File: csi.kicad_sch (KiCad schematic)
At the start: 5 parts, among them J6 WE_68715014022

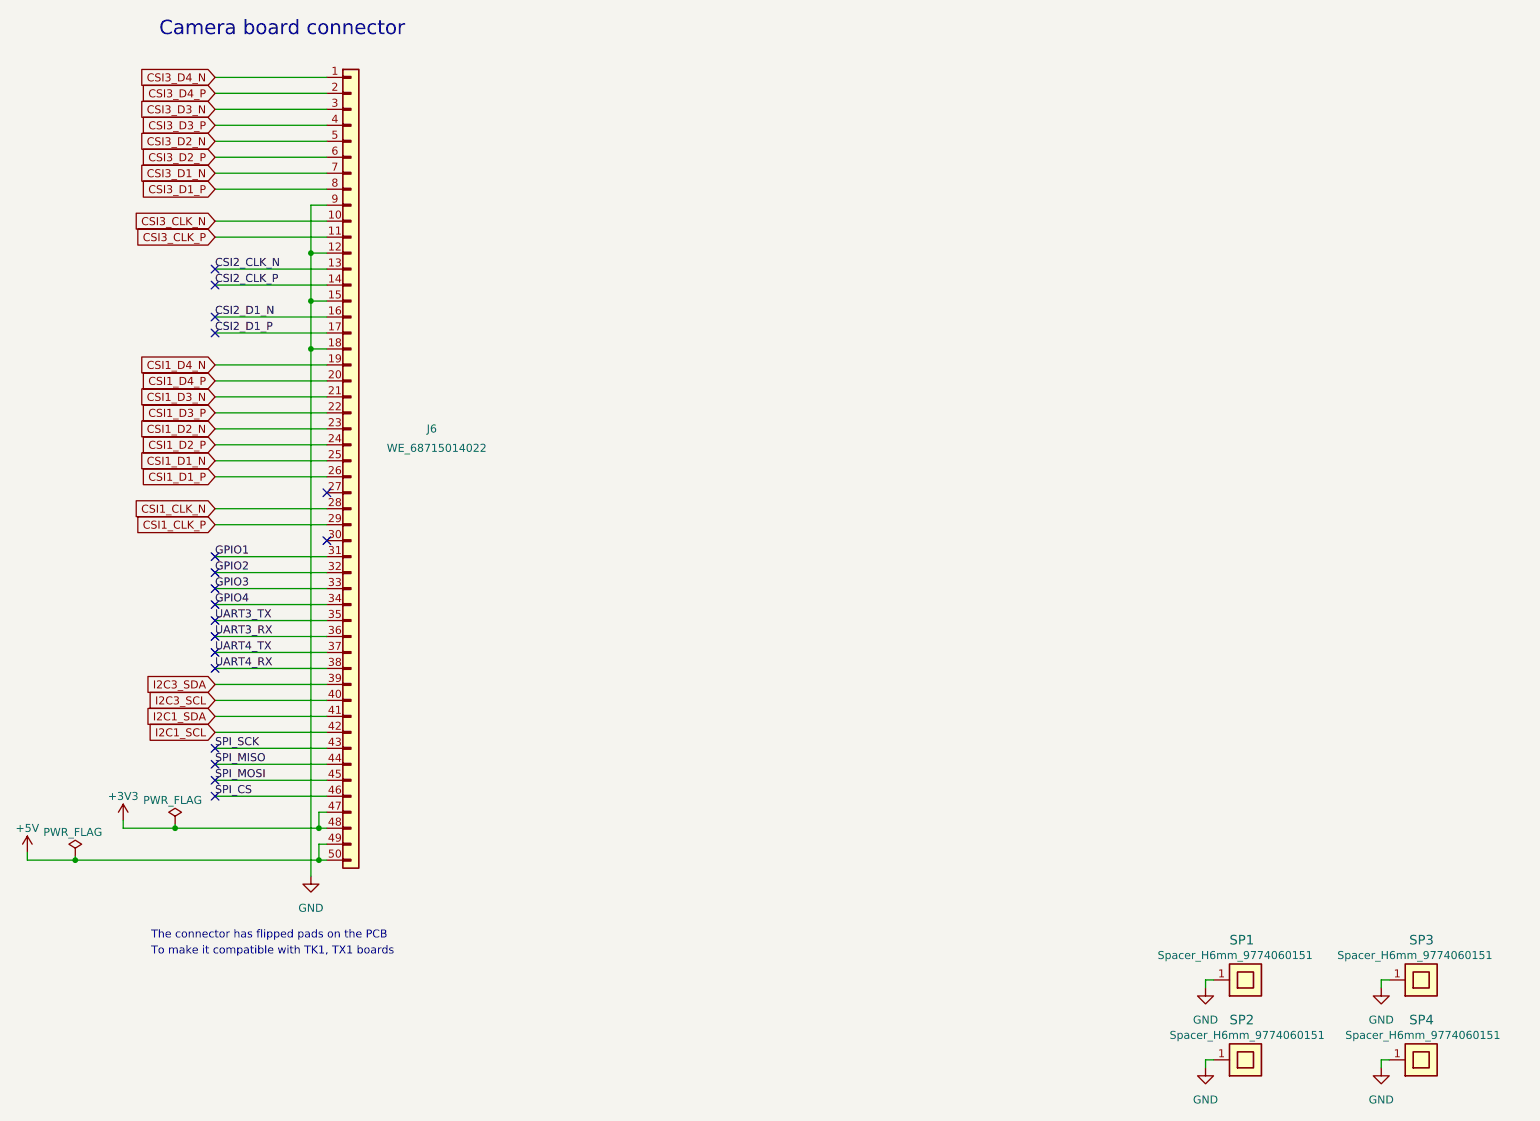
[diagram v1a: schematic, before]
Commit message: [#58304] Update symbols to global libs
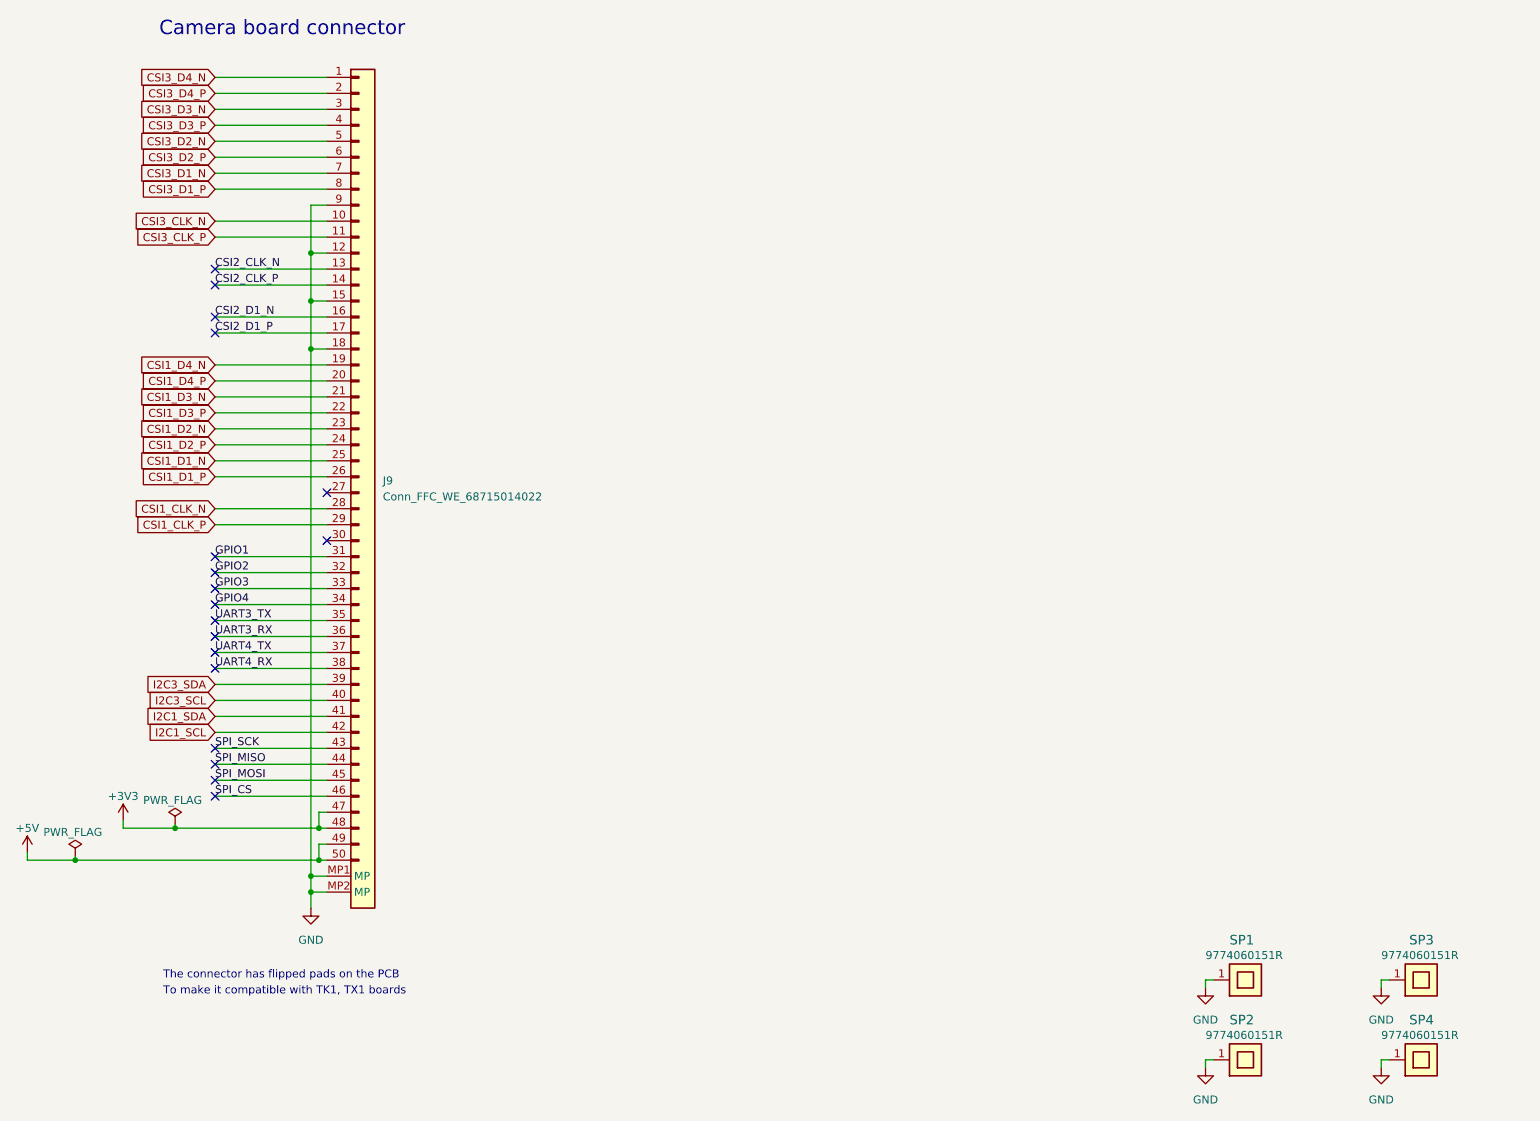
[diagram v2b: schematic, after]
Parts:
- removed J6: WE_68715014022, antmicro-hdmi-mipi-bridge-hw-footprints:WE_68715014022, symbol antmicro-hdmi-mipi-bridge-hw:WE_68715014022
- added J9: Conn_FFC_WE_68715014022, antmicro-footprints:Conn_FFC_WE_68715014x22, symbol antmicroFCCConnectors:Conn_FFC_WE_68715014022
- SP1, SP2, SP3, SP4: value Spacer_H6mm_9774060151 -> Spacer_Drill3.7mm_H6mm_9774060151R; footprint antmicro-hdmi-mipi-bridge-hw-footprints:Spacer_SMD_M2.5_H6mm_Wurth_9774060151 -> antmicro-footprints:Spacer_Drill3.7mm_H6mm_9774060151R; symbol antmicro-hdmi-mipi-bridge-hw:Spacer_H6mm_9774060151 -> antmicroMechanicalParts:Spacer_Drill3.7mm_H6mm_9774060151R; MPN 9774060151 -> 9774060151R
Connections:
- net +3V3: now also J9.47, J9.48
- net +5V: now also J9.49, J9.50
- net CSI1_CLK_N: now also J9.28
- net CSI1_CLK_P: now also J9.29
- net CSI1_D1_N: now also J9.25
- net CSI1_D1_P: now also J9.26
- net CSI1_D2_N: now also J9.23
- net CSI1_D2_P: now also J9.24
- net CSI1_D3_N: now also J9.21
- net CSI1_D3_P: now also J9.22
- net CSI1_D4_N: now also J9.19
- net CSI1_D4_P: now also J9.20
- net CSI2_CLK_N: now also J9.13
- net CSI2_CLK_P: now also J9.14
- net CSI2_D1_N: now also J9.16
- net CSI2_D1_P: now also J9.17
- net CSI3_CLK_N: now also J9.10
- net CSI3_CLK_P: now also J9.11
- net CSI3_D1_N: now also J9.7
- net CSI3_D1_P: now also J9.8
- net CSI3_D2_N: now also J9.5
- net CSI3_D2_P: now also J9.6
- net CSI3_D3_N: now also J9.3
- net CSI3_D3_P: now also J9.4
- net CSI3_D4_N: now also J9.1
- net CSI3_D4_P: now also J9.2
- net GND: now also J9.12, J9.15, J9.18, J9.9, J9.MP1 (MP), J9.MP2 (MP)
- net GPIO1: now also J9.31
- net GPIO2: now also J9.32
- net GPIO3: now also J9.33
- net GPIO4: now also J9.34
- net I2C1_SCL: now also J9.42
- net I2C1_SDA: now also J9.41
- net I2C3_SCL: now also J9.40
- net I2C3_SDA: now also J9.39
- net SPI_CS: now also J9.46
- net SPI_MISO: now also J9.44
- net SPI_MOSI: now also J9.45
- net SPI_SCK: now also J9.43
- net UART3_RX: now also J9.36
- net UART3_TX: now also J9.35
- net UART4_RX: now also J9.38
- net UART4_TX: now also J9.37

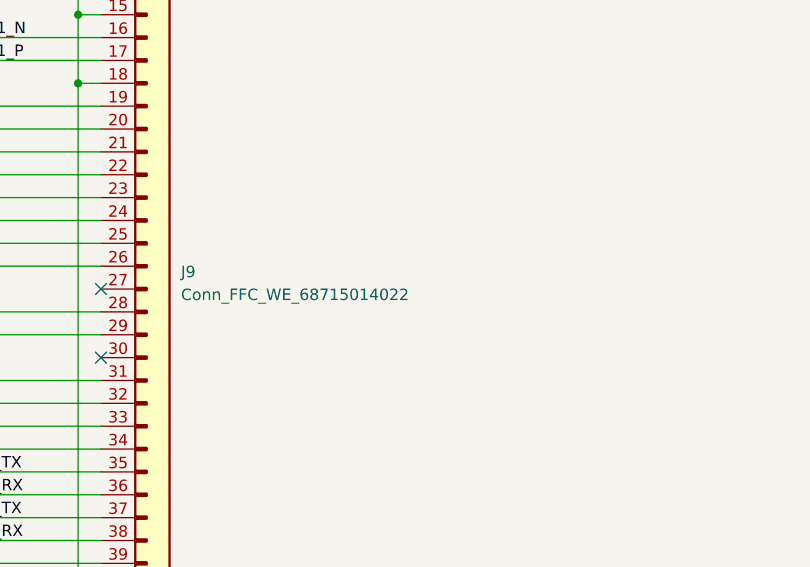
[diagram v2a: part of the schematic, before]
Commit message: [#58304] Change J6 to Conn_FFC_WE_68715014x22_CUSTOM_FLIPPED
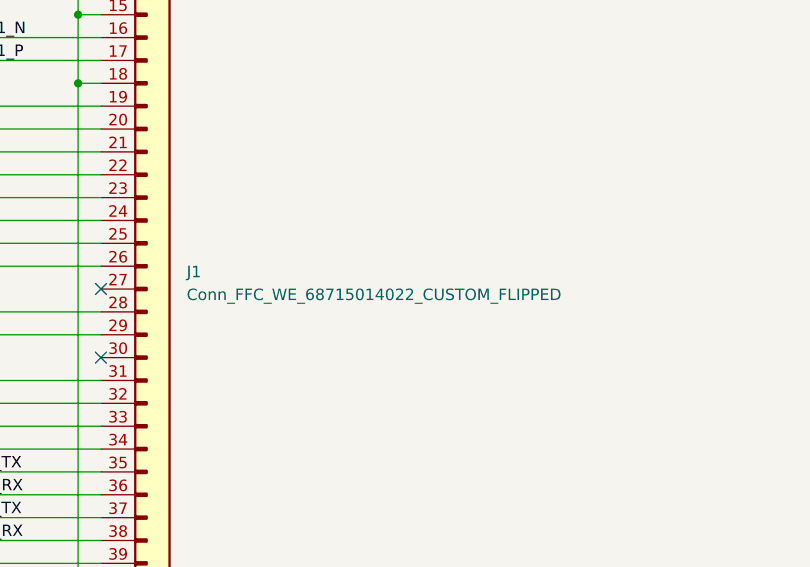
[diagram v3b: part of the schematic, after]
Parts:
- removed J9: Conn_FFC_WE_68715014022, antmicro-footprints:Conn_FFC_WE_68715014x22, symbol antmicroFCCConnectors:Conn_FFC_WE_68715014022
- added J1: Conn_FFC_WE_68715014022_CUSTOM_FLIPPED, antmicro-footprints:Conn_FFC_WE_68715014x22_CUSTOM_FLIPPED, symbol antmicroFCCConnectors:Conn_FFC_WE_68715014022_CUSTOM_FLIPPED
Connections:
- net +3V3: now also J1.47, J1.48
- net +5V: now also J1.49, J1.50
- net CSI1_CLK_N: now also J1.28
- net CSI1_CLK_P: now also J1.29
- net CSI1_D1_N: now also J1.25
- net CSI1_D1_P: now also J1.26
- net CSI1_D2_N: now also J1.23
- net CSI1_D2_P: now also J1.24
- net CSI1_D3_N: now also J1.21
- net CSI1_D3_P: now also J1.22
- net CSI1_D4_N: now also J1.19
- net CSI1_D4_P: now also J1.20
- net CSI2_CLK_N: now also J1.13
- net CSI2_CLK_P: now also J1.14
- net CSI2_D1_N: now also J1.16
- net CSI2_D1_P: now also J1.17
- net CSI3_CLK_N: now also J1.10
- net CSI3_CLK_P: now also J1.11
- net CSI3_D1_N: now also J1.7
- net CSI3_D1_P: now also J1.8
- net CSI3_D2_N: now also J1.5
- net CSI3_D2_P: now also J1.6
- net CSI3_D3_N: now also J1.3
- net CSI3_D3_P: now also J1.4
- net CSI3_D4_N: now also J1.1
- net CSI3_D4_P: now also J1.2
- net GND: now also J1.12, J1.15, J1.18, J1.9, J1.MP1 (MP), J1.MP2 (MP)
- net GPIO1: now also J1.31
- net GPIO2: now also J1.32
- net GPIO3: now also J1.33
- net GPIO4: now also J1.34
- net I2C1_SCL: now also J1.42
- net I2C1_SDA: now also J1.41
- net I2C3_SCL: now also J1.40
- net I2C3_SDA: now also J1.39
- net SPI_CS: now also J1.46
- net SPI_MISO: now also J1.44
- net SPI_MOSI: now also J1.45
- net SPI_SCK: now also J1.43
- net UART3_RX: now also J1.36
- net UART3_TX: now also J1.35
- net UART4_RX: now also J1.38
- net UART4_TX: now also J1.37
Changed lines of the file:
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@@
-    )
-  )
-  (symbol (lib_id "antmicroFCCConnectors:Conn_FFC_WE_68715014022") (at 204.47 82.55 0) (unit 1)
-    (in_bom yes) (on_board yes) (dnp no) (fields_autoplaced)
-    (property "Reference" "J9" (at 213.36 146.685 0)
-      (effects (font (size 1.27 1.27) (thickness 0.15)) (justify left))
-    )
-    (property "Value" "Conn_FFC_WE_68715014022" (at 213.36 149.225 0)
-      (effects (font (size 1.27 1.27) (thickness 0.15)) (justify left))
-    )
-    (property "Footprint" "antmicro-footprints:Conn_FFC_WE_68715014x22" (at 223.52 92.71 0)
-      (effects (font (size 1.27 1.27) (thickness 0.15)) (justify left bottom) hide)
-    )
-    (property "Datasheet" "https://www.we-online.com/components/products/datasheet/68715014022.pdf" (at 223.52 95.25 0)
-      (effects (font (size 1.27 1.27) (thickness 0.15)) (justify left bottom) hide)
-    )
-    (property "MPN" "68715014022" (at 223.52 97.79 0)
-      (effects (font (size 1.27 1.27) (thickness 0.15)) (justify left bottom) hide)
-    )
-    (property "Manufacturer" "Würth Elektronik" (at 223.52 100.33 0)
-      (effects (font (size 1.27 1.27) (thickness 0.15)) (justify left bottom) hide)
-    )
-    (property "Author" "Antmicro" (at 223.52 102.87 0)
-      (effects (font (size 1.27 1.27) (thickness 0.15)) (justify left bottom) hide)
-    )
-    (property "License" "Apache-2.0" (at 223.52 105.41 0)
-      (effects (font (size 1.27 1.27) (thickness 0.15)) (justify left bottom) hide)
-    )
-    (pin "14")
-    (pin "10")
-    (pin "8")
-    (pin "3")
-    (pin "4")
-    (pin "49")
-    (pin "43")
-    (pin "15")
-    (pin "47")
-    (pin "37")
-    (pin "39")
-    (pin "33")
-    (pin "38")
-    (pin "27")
-    (pin "50")
-    (pin "6")
-    (pin "20")
-    (pin "40")
-    (pin "31")
-    (pin "29")
-    (pin "28")
-    (pin "32")
-    (pin "44")
-    (pin "36")
-    (pin "MP2")
-    (pin "9")
-    (pin "30")
-    (pin "16")
-    (pin "41")
-    (pin "23")
-    (pin "22")
-    (pin "5")
-    (pin "35")
-    (pin "MP1")
-    (pin "45")
-    (pin "24")
-    (pin "2")
-    (pin "18")
-    (pin "46")
-    (pin "7")
-    (pin "25")
-    (pin "26")
-    (pin "48")
-    (pin "42")
-    (pin "11")
-    (pin "12")
-    (pin "13")
-    (pin "19")
-    (pin "1")
-    (pin "34")
-    (pin "21")
-    (pin "17")
-    (instances
-      (project "antmicro-hdmi-mipi-bridge-hw"
-        (path "/986e1fb1-d06b-4220-a40c-b0cc1c7adce3/ab3e2e9c-5c2e-4eee-802f-86526e1aed66"
-          (reference "J9") (unit 1)
-        )
-      )
     )
   )
@@
         )
       )
+    )
+  )
+  (symbol (lib_id "antmicroFCCConnectors:Conn_FFC_WE_68715014022_CUSTOM_FLIPPED") (at 204.47 82.55 0) (unit 1)
+    (in_bom yes) (on_board yes) (dnp no) (fields_autoplaced)
+    (property "Reference" "J1" (at 213.995 146.685 0)
+      (effects (font (size 1.27 1.27) (thickness 0.15)) (justify left))
+    )
+    (property "Value" "Conn_FFC_WE_68715014022_CUSTOM_FLIPPED" (at 213.995 149.225 0)
+      (effects (font (size 1.27 1.27) (thickness 0.15)) (justify left))
+    )
+    (property "Footprint" "antmicro-footprints:Conn_FFC_WE_68715014x22_CUSTOM_FLIPPED" (at 223.52 92.71 0)
+      (effects (font (size 1.27 1.27) (thickness 0.15)) (justify left bottom) hide)
+    )
+    (property "Datasheet" "https://www.we-online.com/components/products/datasheet/68715014022.pdf" (at 223.52 95.25 0)
+      (effects (font (size 1.27 1.27) (thickness 0.15)) (justify left bottom) hide)
+    )
+    (property "MPN" "68715014022" (at 223.52 97.79 0)
+      (effects (font (size 1.27 1.27) (thickness 0.15)) (justify left bottom) hide)
+    )
+    (property "Manufacturer" "Würth Elektronik" (at 223.52 100.33 0)
+      (effects (font (size 1.27 1.27) (thickness 0.15)) (justify left bottom) hide)
+    )
+    (property "Author" "Antmicro" (at 223.52 102.87 0)
+      (effects (font (size 1.27 1.27) (thickness 0.15)) (justify left bottom) hide)
+    )
+    (property "License" "Apache-2.0" (at 223.52 105.41 0)
+      (effects (font (size 1.27 1.27) (thickness 0.15)) (justify left bottom) hide)
+    )
+    (pin "34")
+    (pin "46")
+    (pin "43")
+    (pin "23")
+    (pin "12")
+    (pin "38")
+    (pin "48")
+    (pin "47")
+    (pin "45")
+    (pin "44")
+    (pin "9")
+    (pin "MP1")
+    (pin "16")
+    (pin "42")
+    (pin "49")
+    (pin "32")
+    (pin "31")
+    (pin "2")
+    (pin "41")
+    (pin "11")
+    (pin "40")
+    (pin "4")
+    (pin "28")
+    (pin "25")
+    (pin "18")
+    (pin "39")
+    (pin "29")
+    (pin "8")
+    (pin "1")
+    (pin "5")
+    (pin "6")
+    (pin "24")
+    (pin "3")
+    (pin "7")
+    (pin "13")
+    (pin "33")
+    (pin "30")
+    (pin "10")
+    (pin "MP2")
+    (pin "17")
+    (pin "22")
+    (pin "21")
+    (pin "14")
+    (pin "35")
+    (pin "50")
+    (pin "26")
+    (pin "37")
+    (pin "20")
+    (pin "36")
+    (pin "15")
+    (pin "19")
+    (pin "27")
+    (instances
+      (project "antmicro-hdmi-mipi-bridge-hw"
+        (path "/986e1fb1-d06b-4220-a40c-b0cc1c7adce3/ab3e2e9c-5c2e-4eee-802f-86526e1aed66"
+          (reference "J1") (unit 1)
+        )
+      )
